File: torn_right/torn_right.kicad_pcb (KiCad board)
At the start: 2 copper layers, 140.7 x 115.4 mm, 64 parts, among them J2 SJ-43514, J3 Conn_01x04, SW23 SW_Push, SW24 SW_Push, SW25 SW_Push, SW26 SW_Push, SW27 SW_Push, SW28 Rotary_Encoder_Switch, SW29 SW_Push, SW30 SW_Push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

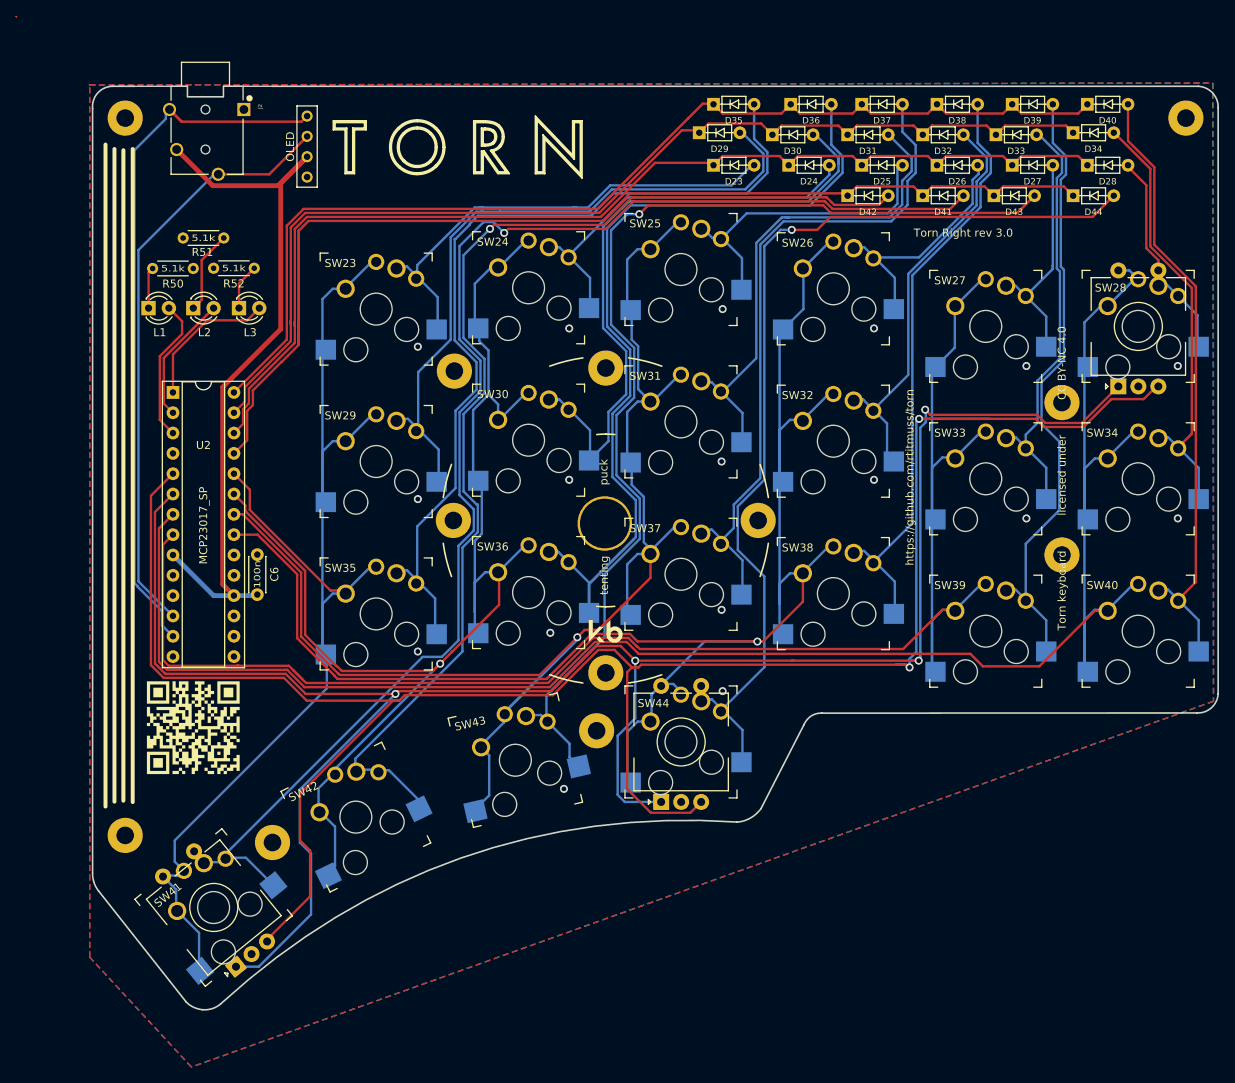
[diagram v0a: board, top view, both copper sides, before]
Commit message: switched out SJ-43514 TRRS jack connector for PJ-320A
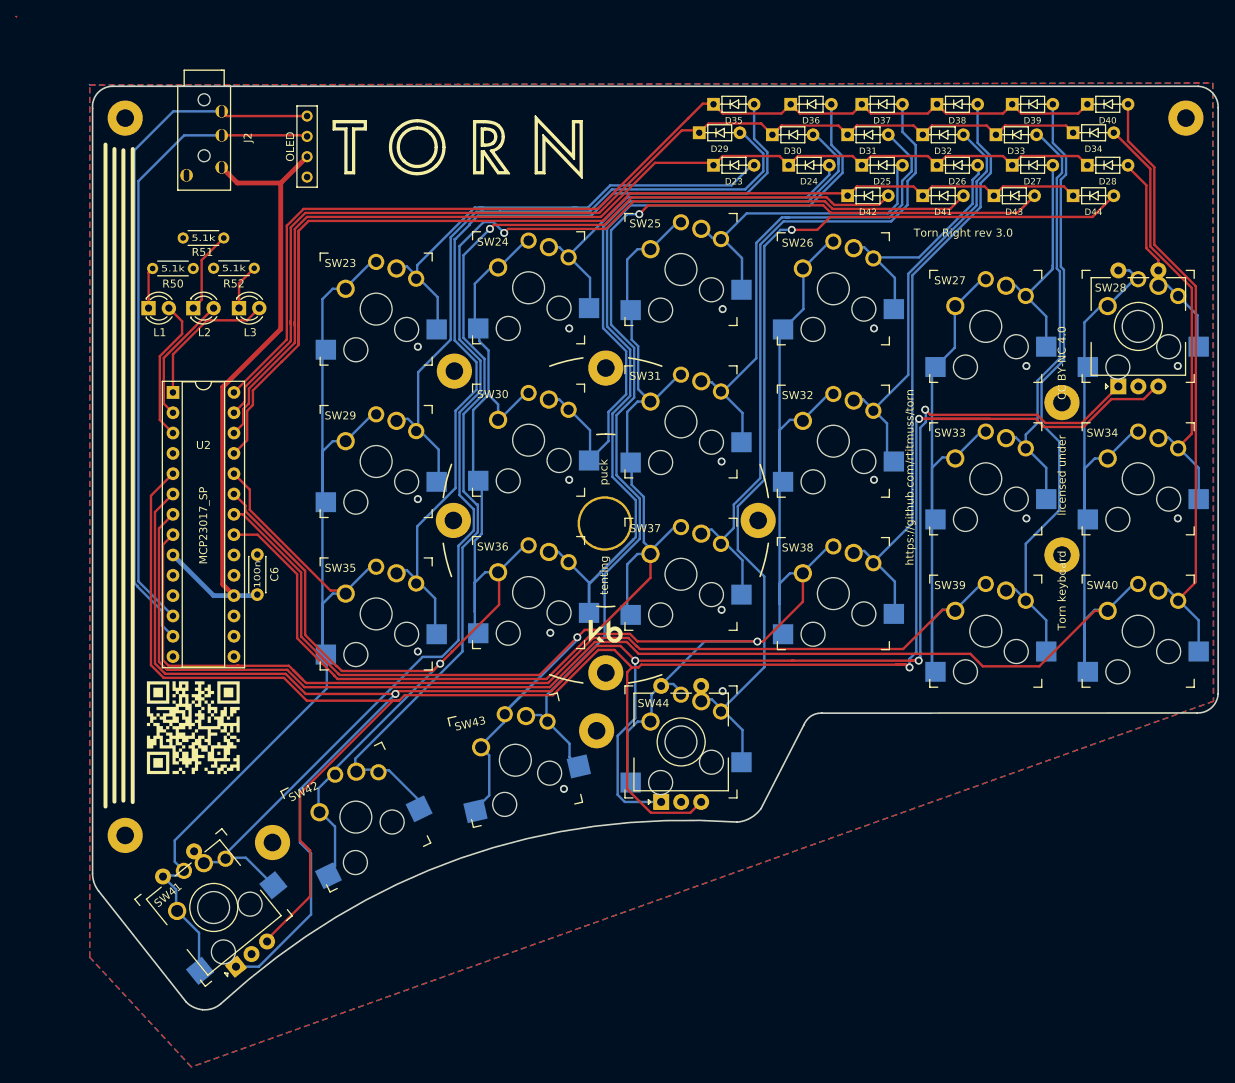
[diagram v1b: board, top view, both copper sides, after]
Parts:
- J2: footprint footprints:CUI_SJ-43514 -> footprints:PJ-320A
- moved J2 7.79 mm to (66.3, 48.4)
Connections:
- U2 pad 11: (no net) -> Net-(U2-Pad11)
- U2 pad 14: (no net) -> Net-(U2-Pad14)
- U2 pad 19: (no net) -> Net-(U2-Pad19)
- U2 pad 20: (no net) -> Net-(U2-Pad20)
- U2 pad 4: (no net) -> Net-(U2-Pad4)
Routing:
- net +5V: track 92.4 -> 80.9 mm
- net /i2c_SCL: track 74.3 -> 79.6 mm
- net /i2c_SDA: track 90.4 -> 86.6 mm
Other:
- outline, holes or cut-outs redrawn
